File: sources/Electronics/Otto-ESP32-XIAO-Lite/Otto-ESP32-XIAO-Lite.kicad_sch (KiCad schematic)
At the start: 21 parts, among them J1 Conn_01x03, J10 Conn_01x02, J12 OLED 0,91" - I2C (SKU21796), J13 MPU6050, J2 Conn_01x03, J3 Conn_01x03, J4 Conn_01x03, J5 Conn_01x03, J6 Conn_01x03, J7 Ultrasonic sensor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

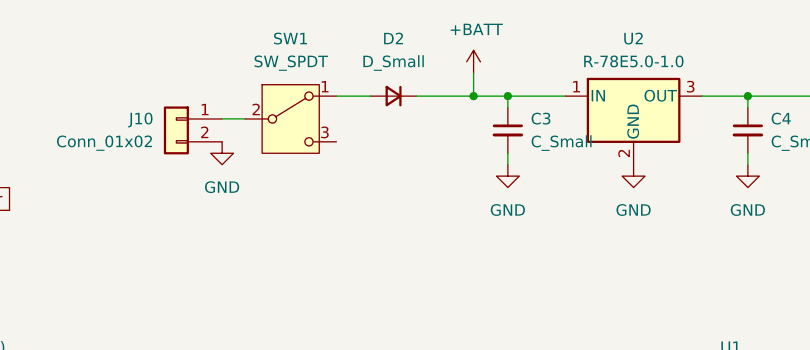
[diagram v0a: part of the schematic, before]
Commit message: New version
- Add pinout servo documentation
- Remove diode D2
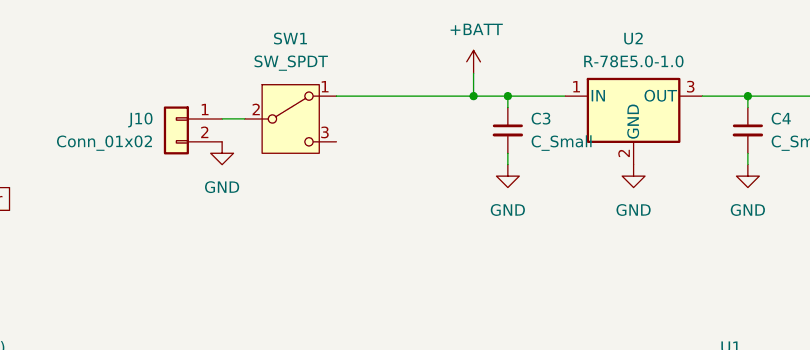
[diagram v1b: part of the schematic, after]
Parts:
- removed D2: D_Small, Diode_THT:D_A-405_P7.62mm_Horizontal, symbol Device:D_Small
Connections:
- net +BATT: now also SW1.1 (A)
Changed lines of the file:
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@@
-	(wire
-		(pts
-			(xy 111.76 41.91) (xy 118.11 41.91)
-		)
-		(stroke
-			(width 0)
-			(type default)
-		)
-	)
 	(wire
 		(pts
@@
 	(wire
 		(pts
-			(xy 102.87 41.91) (xy 106.68 41.91)
+			(xy 102.87 41.91) (xy 118.11 41.91)
 		)
 		(stroke
@@
 					(unit 1)
 				)
-			)
-		)
-	)
-	(symbol
-		(lib_id "Device:D_Small")
-		(at 109.22 41.91 180)
-		(unit 1)
-		(exclude_from_sim no)
-		(in_bom yes)
-		(on_board yes)
-		(dnp no)
-		(fields_autoplaced yes)
-		(property "Reference" "D2"
-			(at 109.22 35.56 0)
-			(effects
-				(font
-					(size 1.27 1.27)
-				)
-			)
-		)
-		(property "Value" "D_Small"
-			(at 109.22 38.1 0)
-			(effects
-				(font
-					(size 1.27 1.27)
-				)
-			)
-		)
-		(property "Footprint" "Diode_THT:D_A-405_P7.62mm_Horizontal"
-			(at 109.22 41.91 90)
-			(effects
-				(font
-					(size 1.27 1.27)
-				)
-				(hide yes)
-			)
-		)
-		(property "Datasheet" "~"
-			(at 109.22 41.91 90)
-			(effects
-				(font
-					(size 1.27 1.27)
-				)
-				(hide yes)
-			)
-		)
-		(property "Description" "Diode, small symbol"
-			(at 109.22 41.91 0)
-			(effects
-				(font
-					(size 1.27 1.27)
-				)
-				(hide yes)
-			)
-		)
-		(property "Sim.Device" "D"
-			(at 109.22 41.91 0)
-			(effects
-				(font
-					(size 1.27 1.27)
-				)
-				(hide yes)
-			)
-		)
-		(property "Sim.Pins" "1=K 2=A"
-			(at 109.22 41.91 0)
-			(effects
-				(font
-					(size 1.27 1.27)
-				)
-				(hide yes)
-			)
-		)
-		(pin "2"
-		)
-		(pin "1"
-		)
-		(instances
-			(project "Otto-ESP32-XIAO-Lite"
-				(path "/d2682c99-4285-4c0b-9e61-08b763b3ce0d"
-					(reference "D2")
-					(unit 1)
-				)

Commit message: update documentation
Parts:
- C3, C4: value C_Small -> 10uF 25V
- D1: value LED_Small -> 5mm Red
- D4: value D_Schottky -> 1N5819
- J1: value Conn_01x03 -> Servo_01
- J10: value Conn_01x02 -> JST
- J2: value Conn_01x03 -> Servo_02
- J3: value Conn_01x03 -> Servo_03
- J4: value Conn_01x03 -> Servo_04
- J5: value Conn_01x03 -> Servo_05
- J6: value Conn_01x03 -> Servo_06
- R1: value R_Small -> 1K
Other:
- note added: "5V max 1A max"
- note added: "ADDONS"
- note added: "BUZZER"
- note added: "CAPTEUR ULTRASON"
- note added: "ENSEMBLE ALIMENTATION"
- note added: "HC-SR04"
- note added: "I2C addons pour ecrans, capteurs et étendeurs I2C"
- note added: "MICROCONTROLEUR"
- note added: "Module XIAO-ESP32C3"
- note added: "SERVOMOTEURS"
- company: (none) -> UniLaSalle Amiens - MakerSpace
- title: (none) -> PCB Otto Mks
- moved on the sheet: BZ1, C3, C4, D1, D4, J1, J10, J12, J13, J2, J3, J4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

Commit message: add header pin option for XIAO
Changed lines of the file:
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@@
 (kicad_sch
-	(version 20231120)
+	(version 20250114)
 	(generator "eeschema")
-	(generator_version "8.0")
+	(generator_version "9.0")
 	(paper "A5")
 	(title_block
@@
 		(comment 3 "https://github.com/Makerspace-Amiens/otto-mks")
 	)
+	(rectangle
+		(start 31.75 85.09)
+		(end 88.9 120.65)
+		(stroke
+			(width 0)
+			(type default)
+		)
+		(fill
+			(type none)
+		)
+	)
+	(rectangle
+		(start 57.15 17.78)
+		(end 88.9 83.82)
+		(stroke
+			(width 0)
+			(type default)
+		)
+		(fill
+			(type none)
+		)
+	)
+	(rectangle
+		(start 90.17 52.07)
+		(end 175.26 102.87)
+		(stroke
+			(width 0)
+			(type default)
+		)
+		(fill
+			(type none)
+		)
+	)
+	(rectangle
+		(start 31.75 17.78)
+		(end 55.88 54.61)
+		(stroke
+			(width 0)
+			(type default)
+		)
+		(fill
+			(type none)
+		)
+	)
+	(rectangle
+		(start 90.17 17.78)
+		(end 175.26 50.8)
+		(stroke
+			(width 0)
+			(type default)
+		)
+		(fill
+			(type none)
+		)
+	)
+	(rectangle
+		(start 31.75 55.88)
+		(end 55.88 83.82)
+		(stroke
+			(width 0)
+			(type default)
+		)
+		(fill
+			(type none)
+		)
+	)
+	(text "HC-SR04"
+		(exclude_from_sim no)
+		(at 32.512 23.368 0)
+		(effects
+			(font
+				(size 1.016 1.016)
+			)
+			(justify left)
+		)
+	)
+	(text "CAPTEUR ULTRASON"
+		(exclude_from_sim no)
+		(at 32.258 20.066 0)
+		(effects
+			(font
+				(size 1.27 1.27)
+				(thickness 0.254)
+				(bold yes)
+			)
+			(justify left)
+		)
+	)
+	(text "BUZZER"
+		(exclude_from_sim no)
+		(at 32.258 58.166 0)
+		(effects
+			(font
+				(size 1.27 1.27)
+				(thickness 0.254)
+				(bold yes)
+			)
+			(justify left)
+		)
+	)
+	(text "ADDONS"
+		(exclude_from_sim no)
+		(at 32.258 87.376 0)
+		(effects
+			(font
+				(size 1.27 1.27)
+				(thickness 0.254)
+				(bold yes)
+			)
+			(justify left)
+		)
+	)
+	(text "ENSEMBLE ALIMENTATION"
+		(exclude_from_sim no)
+		(at 90.678 20.066 0)
+		(effects
+			(font
+				(size 1.27 1.27)
+				(thickness 0.254)
+				(bold yes)
+			)
+			(justify left)
+		)
+	)
+	(text "SERVOMOTEURS\n"
+		(exclude_from_sim no)
+		(at 57.658 20.066 0)
+		(effects
+			(font
+				(size 1.27 1.27)
+				(thickness 0.254)
+				(bold yes)
+			)
+			(justify left)
+		)
+	)
+	(text "Module XIAO-ESP32C3"
+		(exclude_from_sim no)
+		(at 90.932 57.658 0)
+		(effects
+			(font
+				(size 1.016 1.016)
+			)
+			(justify left)
+		)
+	)
+	(text "I2C addons pour ecrans, capteurs et étendeurs I2C"
+		(exclude_from_sim no)
+		(at 32.512 90.678 0)
+		(effects
+			(font
+				(size 1.016 1.016)
+			)
+			(justify left)
+		)
+	)
+	(text "MICROCONTROLEUR"
+		(exclude_from_sim no)
+		(at 90.678 54.356 0)
+		(effects
+			(font
+				(size 1.27 1.27)
+				(thickness 0.254)
+				(bold yes)
+			)
+			(justify left)
+		)
+	)
+	(text "5V max\n1A max"
+		(exclude_from_sim no)
+		(at 57.912 24.13 0)
+		(effects
+			(font
+				(size 1.016 1.016)
+			)
+			(justify left)
+		)
+	)
 	(junction
 		(at 124.46 33.02)
@@
 		)
 	)
-	(rectangle
-		(start 31.75 85.09)
-		(end 88.9 120.65)
-		(stroke
-			(width 0)
-			(type default)
-		)
-		(fill
-			(type none)
-		)
-	)
-	(rectangle
-		(start 57.15 17.78)
-		(end 88.9 83.82)
-		(stroke
-			(width 0)
-			(type default)
-		)
-		(fill
-			(type none)
-		)
-	)
-	(rectangle
-		(start 90.17 52.07)
-		(end 175.26 102.87)
-		(stroke
-			(width 0)
-			(type default)
-		)
-		(fill
-			(type none)
-		)
-	)
-	(rectangle
-		(start 31.75 17.78)
-		(end 55.88 54.61)
-		(stroke
-			(width 0)
-			(type default)
-		)
-		(fill
-			(type none)
-		)
-	)
-	(rectangle
-		(start 90.17 17.78)
-		(end 175.26 50.8)
-		(stroke
-			(width 0)
-			(type default)
-		)
-		(fill
-			(type none)
-		)
-	)
-	(rectangle
-		(start 31.75 55.88)
-		(end 55.88 83.82)
-		(stroke
-			(width 0)
-			(type default)
-		)
-		(fill
-			(type none)
-		)
-	)
-	(text "HC-SR04"
-		(exclude_from_sim no)
-		(at 32.512 23.368 0)
-		(effects
-			(font
-				(size 1.016 1.016)
-			)
-			(justify left)
-		)
-	)
-	(text "CAPTEUR ULTRASON"
-		(exclude_from_sim no)
-		(at 32.258 20.066 0)
-		(effects
-			(font
-				(size 1.27 1.27)
-				(thickness 0.254)
-				(bold yes)
-			)
-			(justify left)
-		)
-	)
-	(text "BUZZER"
-		(exclude_from_sim no)
-		(at 32.258 58.166 0)
-		(effects
-			(font
-				(size 1.27 1.27)
-				(thickness 0.254)
-				(bold yes)
-			)
-			(justify left)
-		)
-	)
-	(text "ADDONS"
-		(exclude_from_sim no)
-		(at 32.258 87.376 0)
-		(effects
-			(font
-				(size 1.27 1.27)
-				(thickness 0.254)
-				(bold yes)
-			)
-			(justify left)
-		)
-	)
-	(text "ENSEMBLE ALIMENTATION"
-		(exclude_from_sim no)
-		(at 90.678 20.066 0)
-		(effects
-			(font
-				(size 1.27 1.27)
-				(thickness 0.254)
-				(bold yes)
-			)
-			(justify left)
-		)
-	)
-	(text "SERVOMOTEURS\n"
-		(exclude_from_sim no)
-		(at 57.658 20.066 0)
-		(effects
-			(font
-				(size 1.27 1.27)
-				(thickness 0.254)
-				(bold yes)
-			)
-			(justify left)
-		)
-	)
-	(text "Module XIAO-ESP32C3"
-		(exclude_from_sim no)
-		(at 90.932 57.658 0)
-		(effects
-			(font
-				(size 1.016 1.016)
-			)
-			(justify left)
-		)
-	)
-	(text "I2C addons pour ecrans, capteurs et étendeurs I2C"
-		(exclude_from_sim no)
-		(at 32.512 90.678 0)
-		(effects
-			(font
-				(size 1.016 1.016)
-			)
-			(justify left)
-		)
-	)
-	(text "MICROCONTROLEUR"
-		(exclude_from_sim no)
-		(at 90.678 54.356 0)
-		(effects
-			(font
-				(size 1.27 1.27)
-				(thickness 0.254)
-				(bold yes)
-			)
-			(justify left)
-		)
-	)
-	(text "5V max\n1A max"
-		(exclude_from_sim no)
-		(at 57.912 24.13 0)
-		(effects
-			(font
-				(size 1.016 1.016)
-			)
-			(justify left)
-		)
-	)
 	(global_label "SCL"
 		(shape input)
@@
 		)
 	)
+	(embedded_fonts no)
 )
